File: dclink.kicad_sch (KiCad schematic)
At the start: 1 part

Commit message: done the first half, TODO: logo, connectors
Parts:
- gave numbers to parts that had none: 1
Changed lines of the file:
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@@
   (symbol (lib_id "dcbk310:dcb-310") (at 148.59 113.03 0) (unit 1)
     (in_bom yes) (on_board yes) (fields_autoplaced)
-    (property "Reference" "U?" (id 0) (at 147.066 93.98 0))
+    (property "Reference" "U1" (id 0) (at 147.066 93.98 0))
     (property "Value" "dcb-310" (id 1) (at 147.066 96.52 0))
     (property "Footprint" "dcbk310:dcb-k310" (id 2) (at 148.082 119.126 0)
@@
   (symbol_instances
     (path "/cacc113d-885e-464c-bed1-96200200e5f6"
-      (reference "U?") (unit 1) (value "dcb-310") (footprint "dcbk310:dcb-k310")
+      (reference "U1") (unit 1) (value "dcb-310") (footprint "dcbk310:dcb-k310")
     )
   )

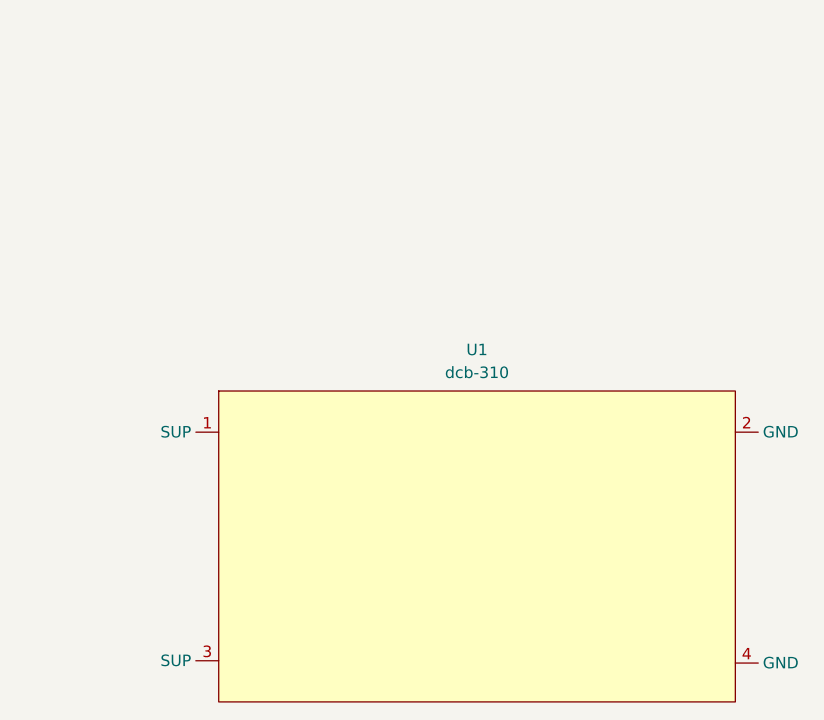
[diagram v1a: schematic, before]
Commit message: new footprint, TODO: pad connections
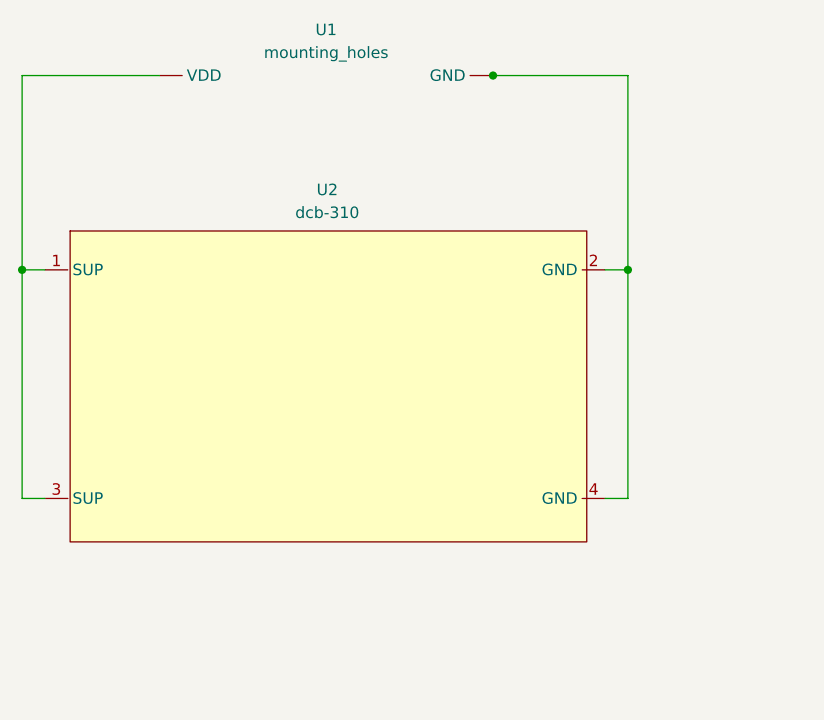
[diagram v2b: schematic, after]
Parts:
- removed U1: dcb-310, dcbk310:dcb-k310, symbol dcbk310:dcb-310
- added U1: mounting_holes, dcbk310:mounting_holes, symbol dcbk310:mounting_holes
- added U2: dcb-310, dcbk310:dcb-k310, symbol dcbk310:dcb-310
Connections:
- new net: U1. (VDD), U2.1 (SUP), U2.3 (SUP)
- new net: U1. (VDD), U2.2 (GND), U2.4 (GND)
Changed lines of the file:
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@@
     (company "E-Agle TRT")
   )
-  (symbol (lib_id "dcbk310:dcb-310") (at 148.59 113.03 0) (unit 1)
+  (junction (at 96.52 85.09) (diameter 0) (color 0 0 0 0)
+  )
+  (junction (at 148.844 63.5) (diameter 0) (color 0 0 0 0)
+  )
+  (junction (at 163.83 85.09) (diameter 0) (color 0 0 0 0)
+  )
+  (wire (pts (xy 163.83 63.5) (xy 163.83 85.09))
+    (stroke (width 0) (type default) (color 0 0 0 0))
+  )
+  (wire (pts (xy 163.83 85.09) (xy 163.83 110.49))
+    (stroke (width 0) (type default) (color 0 0 0 0))
+  )
+  (wire (pts (xy 96.52 110.49) (xy 99.06 110.49))
+    (stroke (width 0) (type default) (color 0 0 0 0))
+  )
+  (wire (pts (xy 148.844 63.5) (xy 163.83 63.5))
+    (stroke (width 0) (type default) (color 0 0 0 0))
+  )
+  (wire (pts (xy 161.29 85.09) (xy 163.83 85.09))
+    (stroke (width 0) (type default) (color 0 0 0 0))
+  )
+  (wire (pts (xy 96.52 63.5) (xy 96.52 85.09))
+    (stroke (width 0) (type default) (color 0 0 0 0))
+  )
+  (wire (pts (xy 96.52 85.09) (xy 99.06 85.09))
+    (stroke (width 0) (type default) (color 0 0 0 0))
+  )
+  (wire (pts (xy 111.76 63.5) (xy 96.52 63.5))
+    (stroke (width 0) (type default) (color 0 0 0 0))
+  )
+  (wire (pts (xy 148.59 63.5) (xy 148.844 63.5))
+    (stroke (width 0) (type default) (color 0 0 0 0))
+  )
+  (wire (pts (xy 96.52 85.09) (xy 96.52 110.49))
+    (stroke (width 0) (type default) (color 0 0 0 0))
+  )
+  (wire (pts (xy 163.83 110.49) (xy 161.29 110.49))
+    (stroke (width 0) (type default) (color 0 0 0 0))
+  )
+  (symbol (lib_id "dcbk310:mounting_holes") (at 128.27 63.5 0) (unit 1)
     (in_bom yes) (on_board yes) (fields_autoplaced)
-    (property "Reference" "U1" (id 0) (at 147.066 93.98 0))
-    (property "Value" "dcb-310" (id 1) (at 147.066 96.52 0))
-    (property "Footprint" "dcbk310:dcb-k310" (id 2) (at 148.082 119.126 0)
+    (property "Reference" "U1" (id 0) (at 130.302 58.42 0))
+    (property "Value" "mounting_holes" (id 1) (at 130.302 60.96 0))
+    (property "Footprint" "dcbk310:mounting_holes" (id 2) (at 128.27 63.5 0)
       (effects (font (size 1.27 1.27)) hide)
     )
-    (property "Datasheet" "" (id 3) (at 164.338 87.376 0)
+    (property "Datasheet" "" (id 3) (at 128.27 63.5 0)
+      (effects (font (size 1.27 1.27)) hide)
+    )
+    (pin "")
+    (pin "")
+  )
+  (symbol (lib_id "dcbk310:dcb-310") (at 132.08 95.25 0) (unit 1)
+    (in_bom yes) (on_board yes) (fields_autoplaced)
+    (property "Reference" "U2" (id 0) (at 130.429 76.2 0))
+    (property "Value" "dcb-310" (id 1) (at 130.429 78.74 0))
+    (property "Footprint" "dcbk310:dcb-k310" (id 2) (at 131.572 101.346 0)
+      (effects (font (size 1.27 1.27)) hide)
+    )
+    (property "Datasheet" "" (id 3) (at 147.828 69.596 0)
       (effects (font (size 1.27 1.27)) hide)
     )
@@
   )
   (symbol_instances
-    (path "/cacc113d-885e-464c-bed1-96200200e5f6"
-      (reference "U1") (unit 1) (value "dcb-310") (footprint "dcbk310:dcb-k310")
+    (path "/3f155697-45a1-4a2b-b40c-d2ef377653ca"
+      (reference "U1") (unit 1) (value "mounting_holes") (footprint "dcbk310:mounting_holes")
+    )
+    (path "/8f6e655b-cbc6-42da-bb7f-c7fcd17f3d2f"
+      (reference "U2") (unit 1) (value "dcb-310") (footprint "dcbk310:dcb-k310")
     )
   )

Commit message: TODO: add vias
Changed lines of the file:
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@@
   (junction (at 96.52 85.09) (diameter 0) (color 0 0 0 0)
-  )
-  (junction (at 148.844 63.5) (diameter 0) (color 0 0 0 0)
   )
   (junction (at 163.83 85.09) (diameter 0) (color 0 0 0 0)
@@
     (stroke (width 0) (type default) (color 0 0 0 0))
   )
-  (wire (pts (xy 148.844 63.5) (xy 163.83 63.5))
+  (wire (pts (xy 161.29 85.09) (xy 163.83 85.09))
     (stroke (width 0) (type default) (color 0 0 0 0))
   )
-  (wire (pts (xy 161.29 85.09) (xy 163.83 85.09))
+  (wire (pts (xy 146.05 63.5) (xy 163.83 63.5))
     (stroke (width 0) (type default) (color 0 0 0 0))
   )
@@
     (stroke (width 0) (type default) (color 0 0 0 0))
   )
-  (wire (pts (xy 148.59 63.5) (xy 148.844 63.5))
-    (stroke (width 0) (type default) (color 0 0 0 0))
-  )
   (wire (pts (xy 96.52 85.09) (xy 96.52 110.49))
     (stroke (width 0) (type default) (color 0 0 0 0))
@@
     (stroke (width 0) (type default) (color 0 0 0 0))
   )
-  (symbol (lib_id "dcbk310:mounting_holes") (at 128.27 63.5 0) (unit 1)
+  (symbol (lib_name "mounting_holes_1") (lib_id "dcbk310:mounting_holes") (at 128.27 63.5 0) (unit 1)
     (in_bom yes) (on_board yes) (fields_autoplaced)
-    (property "Reference" "U1" (id 0) (at 130.302 58.42 0))
-    (property "Value" "mounting_holes" (id 1) (at 130.302 60.96 0))
+    (property "Reference" "U1" (id 0) (at 128.905 58.42 0))
+    (property "Value" "mounting_holes" (id 1) (at 128.905 60.96 0))
     (property "Footprint" "dcbk310:mounting_holes" (id 2) (at 128.27 63.5 0)
       (effects (font (size 1.27 1.27)) hide)
@@
   )
   (symbol_instances
-    (path "/3f155697-45a1-4a2b-b40c-d2ef377653ca"
+    (path "/5b29962f-685a-409c-915c-9c4a92ed442a"
       (reference "U1") (unit 1) (value "mounting_holes") (footprint "dcbk310:mounting_holes")
     )

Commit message: done pad connections
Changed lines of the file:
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@@
     (stroke (width 0) (type default) (color 0 0 0 0))
+  )
+  (symbol (lib_id "power:GND") (at 157.48 63.5 0) (unit 1)
+    (in_bom yes) (on_board yes) (fields_autoplaced)
+    (property "Reference" "#PWR?" (id 0) (at 157.48 69.85 0)
+      (effects (font (size 1.27 1.27)) hide)
+    )
+    (property "Value" "GND" (id 1) (at 157.48 68.58 0))
+    (property "Footprint" "" (id 2) (at 157.48 63.5 0)
+      (effects (font (size 1.27 1.27)) hide)
+    )
+    (property "Datasheet" "" (id 3) (at 157.48 63.5 0)
+      (effects (font (size 1.27 1.27)) hide)
+    )
+    (pin "1")
+  )
+  (symbol (lib_id "power:VDC") (at 102.87 63.5 0) (unit 1)
+    (in_bom yes) (on_board yes) (fields_autoplaced)
+    (property "Reference" "#PWR?" (id 0) (at 102.87 66.04 0)
+      (effects (font (size 1.27 1.27)) hide)
+    )
+    (property "Value" "VDC" (id 1) (at 102.87 58.42 0))
+    (property "Footprint" "" (id 2) (at 102.87 63.5 0)
+      (effects (font (size 1.27 1.27)) hide)
+    )
+    (property "Datasheet" "" (id 3) (at 102.87 63.5 0)
+      (effects (font (size 1.27 1.27)) hide)
+    )
+    (pin "1")
   )
   (symbol (lib_name "mounting_holes_1") (lib_id "dcbk310:mounting_holes") (at 128.27 63.5 0) (unit 1)
@@
   )
   (symbol_instances
+    (path "/06bccb0b-2f4b-4092-834b-3871294199da"
+      (reference "#PWR?") (unit 1) (value "GND") (footprint "")
+    )
+    (path "/119a2ba9-03f2-48af-8f1a-4a96cb25a3bf"
+      (reference "#PWR?") (unit 1) (value "VDC") (footprint "")
+    )
     (path "/5b29962f-685a-409c-915c-9c4a92ed442a"
       (reference "U1") (unit 1) (value "mounting_holes") (footprint "dcbk310:mounting_holes")
